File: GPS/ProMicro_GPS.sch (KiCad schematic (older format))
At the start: 32 parts, among them J1 uFL, J2 Coax, U1 SIM28ML, U2 MPU-9250

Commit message: add 1.8V for Gyro
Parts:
- added C10, C11: 100n, Capacitor_SMD:C_0402_1005Metric, symbol Device:C
- added H1: MountingHole, MountingHole:MountingHole_2.1mm, symbol Mechanical:MountingHole
- added U3: AP2112K-1.8, Package_TO_SOT_SMD:SOT-23-5, symbol Regulator_Linear:AP2112K-1.8
- A1: renamed from A?; symbol MCU_Module:Sparkfun_Pro_Micro_3V3 -> ProMicro:Sparkfun_Pro_Micro_3V3
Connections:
- net +3V3: now also C10.1, U3.1 (VIN), U3.3 (EN); no longer U2.8 (VDDIO)
- net GND: now also C10.2, C11.2, U3.2 (GND)
- new net +1V8: C11.1, U2.8 (VDDIO), U3.5 (VOUT)
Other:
- note removed: "Alternativ:\nICM-20948 requires 1.8V @VDDIO"
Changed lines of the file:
@@
 Title "ProMicro_GPS"
 Date "2020-05-30"
-Rev "v3"
+Rev "v3.1"
 Comp ""
 Comment1 ""
@@
 Wire Wire Line
 	3200 2000 3300 2000
-Wire Wire Line
-	3900 1000 3900 1100
 Wire Wire Line
 	4000 2900 4000 3000
@@
 L power:+3V3 #PWR06
 U 1 1 5E1569C8
-P 3200 1000
-F 0 "#PWR06" H 3200 850 50  0001 C CNN
-F 1 "+3V3" H 3200 1150 50  0000 C CNN
-F 2 "" H 3200 1000 50  0001 C CNN
-F 3 "" H 3200 1000 50  0001 C CNN
-	1    3200 1000
-	1    0    0    -1
-$EndComp
-$Comp
-L power:+3V3 #PWR07
-U 1 1 5E0EC300
-P 3900 1000
-F 0 "#PWR07" H 3900 850 50  0001 C CNN
-F 1 "+3V3" H 3900 1150 50  0000 C CNN
-F 2 "" H 3900 1000 50  0001 C CNN
-F 3 "" H 3900 1000 50  0001 C CNN
-	1    3900 1000
+P 1250 2150
+F 0 "#PWR06" H 1250 2000 50  0001 C CNN
+F 1 "+3V3" H 1250 2300 50  0000 C CNN
+F 2 "" H 1250 2150 50  0001 C CNN
+F 3 "" H 1250 2150 50  0001 C CNN
+	1    1250 2150
 	1    0    0    -1
 $EndComp
@@
 	1    0    0    -1
 $EndComp
-Text Notes 1750 2750 0    50   ~ 0
-Alternativ:\nICM-20948 requires 1.8V @VDDIO
 Text Notes 3250 6750 0    50   ~ 0
 Alternativ:\nMAX-8
@@
 NoConn ~ 8800 2000
 $Comp
-L MCU_Module:Sparkfun_Pro_Micro_3V3 A?
+L ProMicro:Sparkfun_Pro_Micro_3V3 A1
 U 1 1 5F52CC97
 P 8900 3000
-F 0 "A?" H 8900 4200 50  0000 C CNN
-F 1 "Sparkfun_Pro_Micro_3V3" H 8900 4100 50  0000 C CNN
+F 0 "A1" H 8550 3950 50  0000 C CNN
+F 1 "Sparkfun_Pro_Micro_3V3" H 9500 2050 50  0000 C CNN
 F 2 "Module:Sparkfun_Pro_Micro" H 8900 3000 50  0001 C CIN
 F 3 "https://www.sparkfun.com/products/12587" H 8900 2000 50  0001 C CNN
@@
 	1    0    0    -1
 $EndComp
+$Comp
+L power:+1V8 #PWR0103
+U 1 1 5F54927C
+P 2250 2150
+F 0 "#PWR0103" H 2250 2000 50  0001 C CNN
+F 1 "+1V8" H 2250 2300 50  0000 C CNN
+F 2 "" H 2250 2150 50  0001 C CNN
+F 3 "" H 2250 2150 50  0001 C CNN
+	1    2250 2150
+	1    0    0    -1
+$EndComp
+Wire Wire Line
+	3900 1000 3900 1100
+Wire Wire Line
+	1250 2150 1250 2300
+Wire Wire Line
+	1250 2300 1450 2300
+Wire Wire Line
+	2250 2150 2250 2300
+Wire Wire Line
+	2250 2300 2050 2300
+$Comp
+L Device:C C10
+U 1 1 5F551E51
+P 1250 2650
+F 0 "C10" H 1380 2700 50  0000 L CNN
+F 1 "100n" H 1380 2600 50  0000 L CNN
+F 2 "Capacitor_SMD:C_0402_1005Metric" H 1288 2500 50  0001 C CNN
+F 3 "~" H 1250 2650 50  0001 C CNN
+F 4 "CL05B104KO5NNNC" H 1250 2650 50  0001 C CNN "manf#"
+F 5 "GYRO" H 1250 2650 50  0001 C CNN "variant"
+F 6 "C1525" H 1250 2650 50  0001 C CNN "LCSC#"
+	1    1250 2650
+	1    0    0    -1
+$EndComp
+$Comp
+L Device:C C11
+U 1 1 5F552790
+P 2250 2650
+F 0 "C11" H 2380 2700 50  0000 L CNN
+F 1 "100n" H 2380 2600 50  0000 L CNN
+F 2 "Capacitor_SMD:C_0402_1005Metric" H 2288 2500 50  0001 C CNN
+F 3 "~" H 2250 2650 50  0001 C CNN
+F 4 "CL05B104KO5NNNC" H 2250 2650 50  0001 C CNN "manf#"
+F 5 "GYRO" H 2250 2650 50  0001 C CNN "variant"
+F 6 "C1525" H 2250 2650 50  0001 C CNN "LCSC#"
+	1    2250 2650
+	1    0    0    -1
+$EndComp
+$Comp
+L power:GND #PWR0104
+U 1 1 5F552CA6
+P 1250 2900
+F 0 "#PWR0104" H 1250 2650 50  0001 C CNN
+F 1 "GND" H 1250 2750 50  0000 C CNN
+F 2 "" H 1250 2900 50  0001 C CNN
+F 3 "" H 1250 2900 50  0001 C CNN
+	1    1250 2900
+	1    0    0    -1
+$EndComp
+$Comp
+L power:GND #PWR0105
+U 1 1 5F55330E
+P 1750 2900
+F 0 "#PWR0105" H 1750 2650 50  0001 C CNN
+F 1 "GND" H 1750 2750 50  0000 C CNN
+F 2 "" H 1750 2900 50  0001 C CNN
+F 3 "" H 1750 2900 50  0001 C CNN
+	1    1750 2900
+	1    0    0    -1
+$EndComp
+$Comp
+L power:GND #PWR0106
+U 1 1 5F55357B
+P 2250 2900
+F 0 "#PWR0106" H 2250 2650 50  0001 C CNN
+F 1 "GND" H 2250 2750 50  0000 C CNN
+F 2 "" H 2250 2900 50  0001 C CNN
+F 3 "" H 2250 2900 50  0001 C CNN
+	1    2250 2900
+	1    0    0    -1
+$EndComp
+Connection ~ 1250 2300
+Wire Wire Line
+	1250 2900 1250 2800
+Wire Wire Line
+	1750 2700 1750 2900
+Wire Wire Line
+	2250 2900 2250 2800
+Connection ~ 2250 2300
+$Comp
+L power:+1V8 #PWR0107
+U 1 1 5F56BB7F
+P 3900 1000
+F 0 "#PWR0107" H 3900 850 50  0001 C CNN
+F 1 "+1V8" H 3900 1150 50  0000 C CNN
+F 2 "" H 3900 1000 50  0001 C CNN
+F 3 "" H 3900 1000 50  0001 C CNN
+	1    3900 1000
+	1    0    0    -1
+$EndComp
+$Comp
+L power:+3V3 #PWR0108
+U 1 1 5F56BF74
+P 3200 1000
+F 0 "#PWR0108" H 3200 850 50  0001 C CNN
+F 1 "+3V3" H 3200 1150 50  0000 C CNN
+F 2 "" H 3200 1000 50  0001 C CNN
+F 3 "" H 3200 1000 50  0001 C CNN
+	1    3200 1000
+	1    0    0    -1
+$EndComp
+$Comp
+L Regulator_Linear:AP2112K-1.8 U3
+U 1 1 5F56F1F1
+P 1750 2400
+F 0 "U3" H 1775 2800 50  0000 C CNN
+F 1 "AP2112K-1.8" H 1775 2700 50  0000 C CNN
+F 2 "Package_TO_SOT_SMD:SOT-23-5" H 1750 2725 50  0001 C CNN
+F 3 "https://www.diodes.com/assets/Datasheets/AP2112.pdf" H 1750 2500 50  0001 C CNN
+	1    1750 2400
+	1    0    0    -1
+$EndComp
+Wire Wire Line
+	2250 2300 2250 2500
+Wire Wire Line
+	1450 2400 1250 2400
+Wire Wire Line
+	1250 2300 1250 2400
+Wire Wire Line
+	1250 2400 1250 2500
+Connection ~ 1250 2400
+$Comp
+L Mechanical:MountingHole H1
+U 1 1 5F549B76
+P 5750 4750
+F 0 "H1" H 5850 4825 50  0000 L CNN
+F 1 "MountingHole" H 5850 4725 50  0000 L CNN
+F 2 "MountingHole:MountingHole_2.1mm" H 5750 4750 50  0001 C CNN
+F 3 "~" H 5750 4750 50  0001 C CNN
+	1    5750 4750
+	1    0    0    -1
+$EndComp

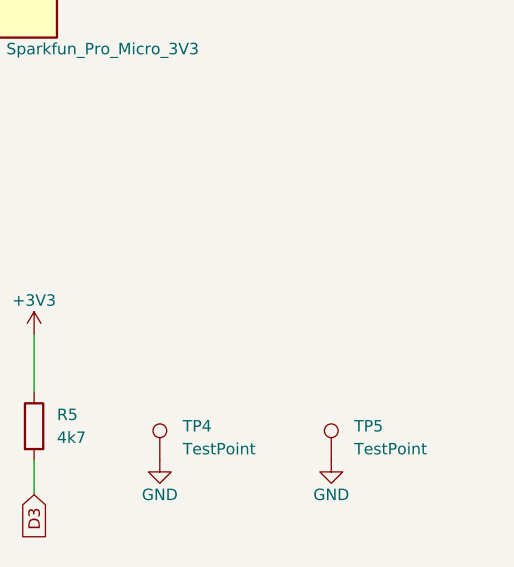
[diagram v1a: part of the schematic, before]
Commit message: adding holes for antenna
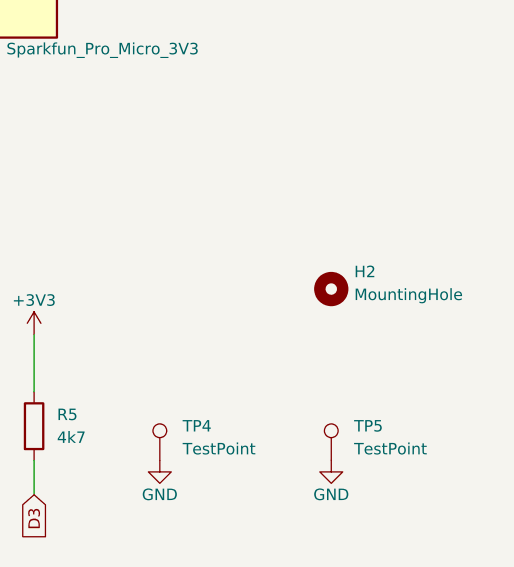
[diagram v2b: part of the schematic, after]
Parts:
- added H2: MountingHole, MountingHole:MountingHole_2.1mm, symbol Mechanical:MountingHole
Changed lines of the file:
@@
 Sheet 1 1
 Title "ProMicro_GPS"
-Date "2020-05-30"
+Date "2020-09-05"
 Rev "v3.1"
 Comp ""
@@
 	1    0    0    -1
 $EndComp
+$Comp
+L Mechanical:MountingHole H2
+U 1 1 5F544468
+P 10500 5000
+F 0 "H2" H 10600 5075 50  0000 L CNN
+F 1 "MountingHole" H 10600 4975 50  0000 L CNN
+F 2 "MountingHole:MountingHole_2.1mm" H 10500 5000 50  0001 C CNN
+F 3 "~" H 10500 5000 50  0001 C CNN
+	1    10500 5000
+	1    0    0    -1
+$EndComp

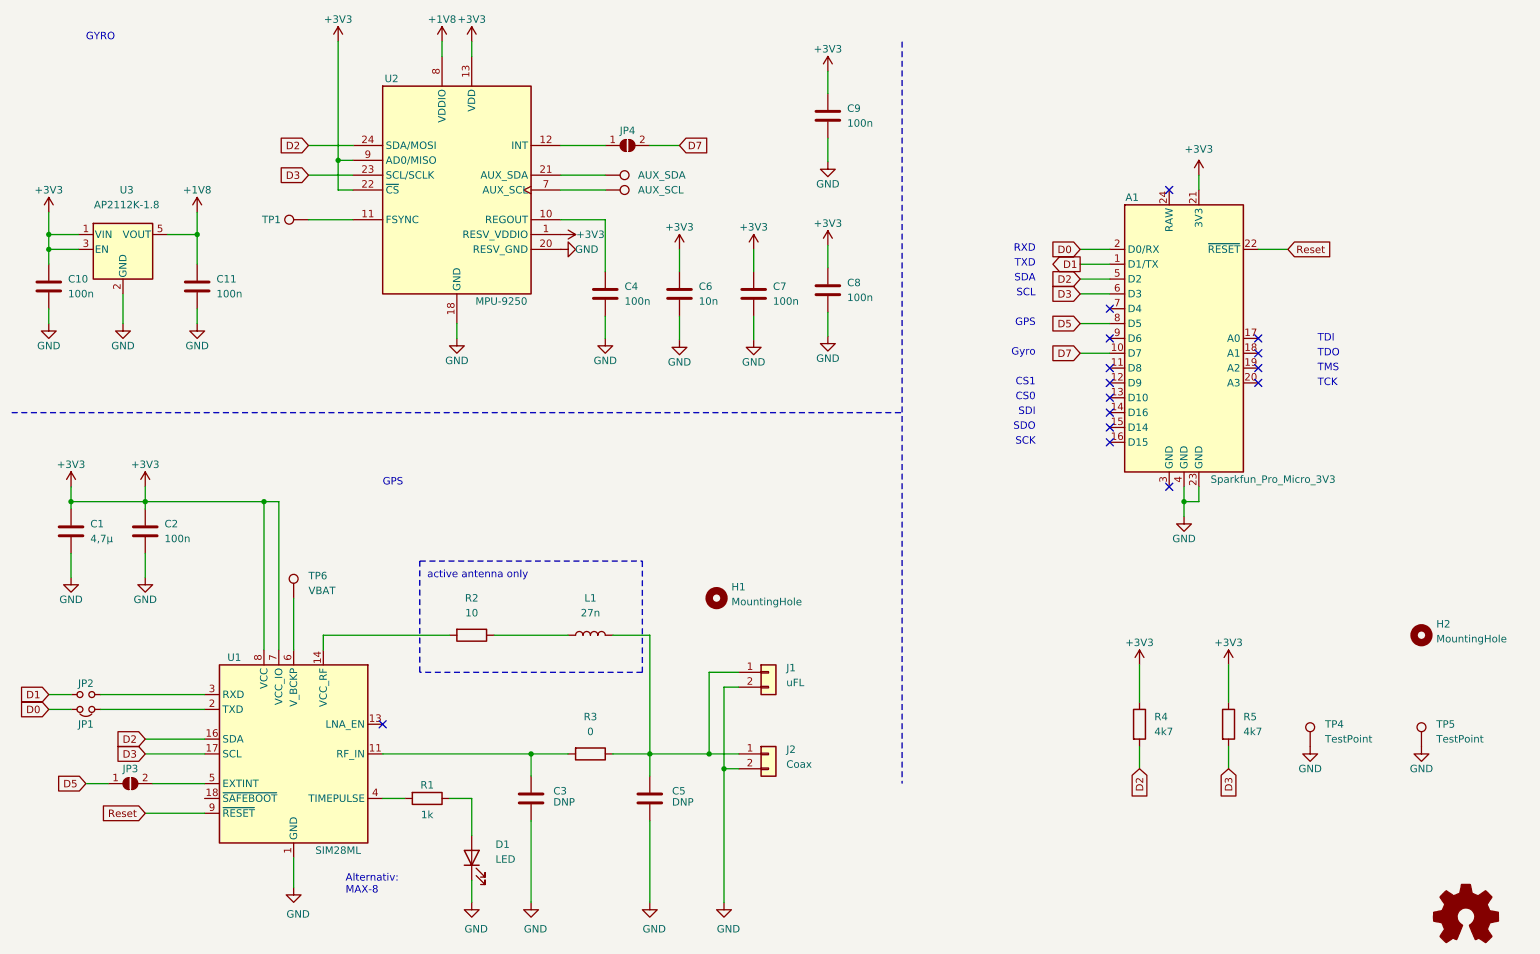
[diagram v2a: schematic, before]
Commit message: changed signal names
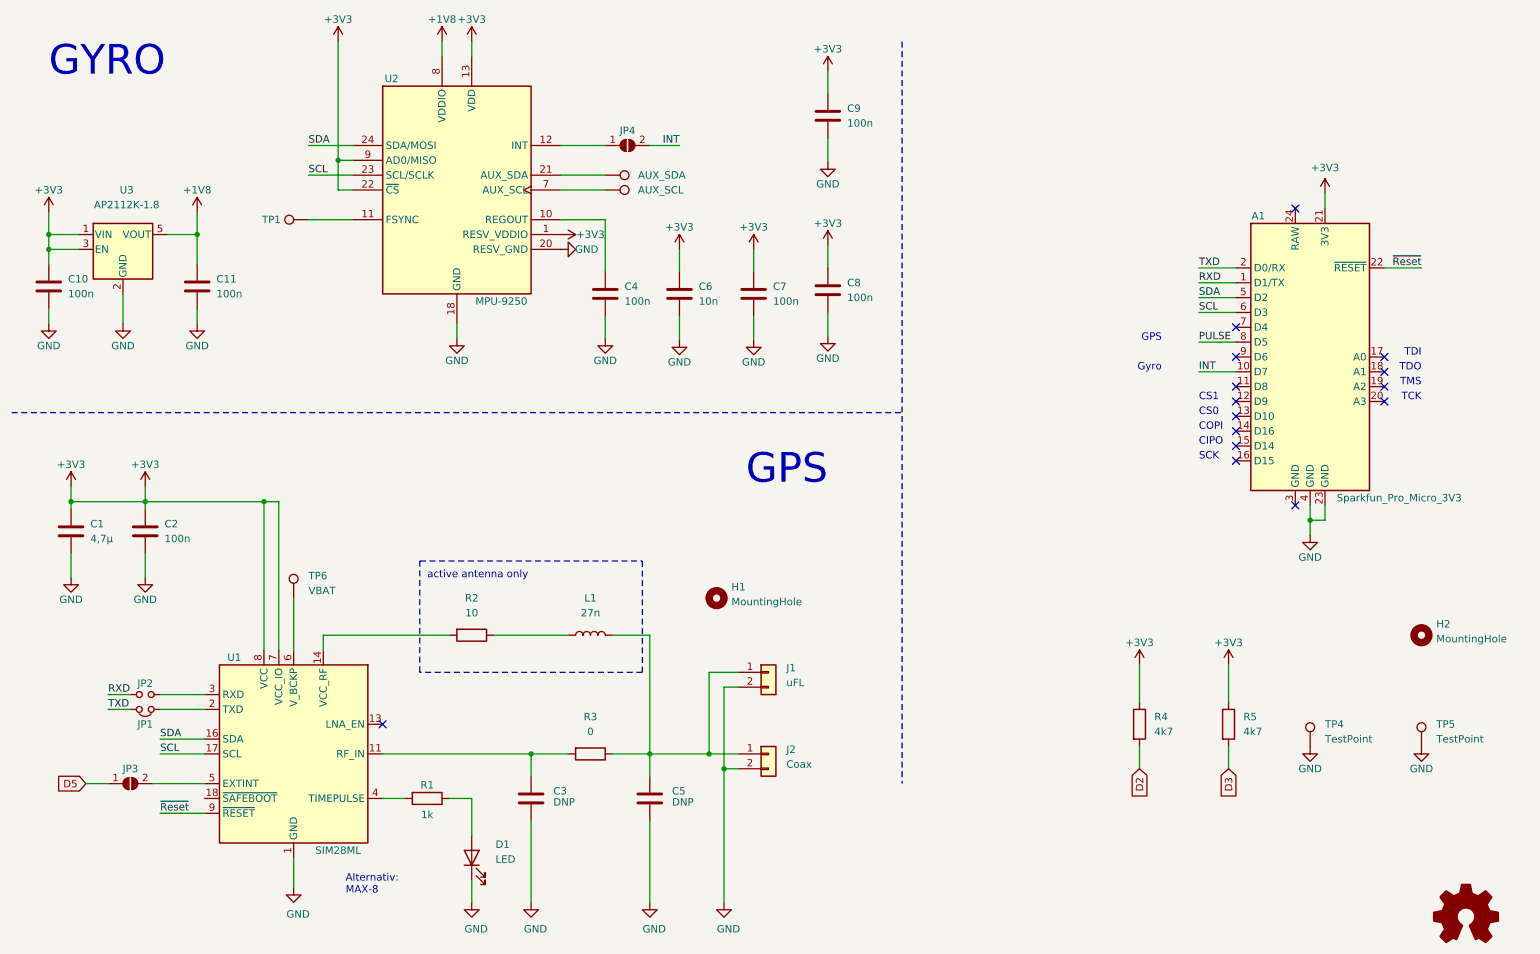
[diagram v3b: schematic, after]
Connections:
- net D2: no longer A1.5 (D2), U1.16 (SDA), U2.24 (SDA/MOSI)
- net D3: no longer A1.6 (D3), U1.17 (SCL), U2.23 (SCL/SCLK)
- net D5: no longer A1.8 (D5)
- net D0 renamed TXD
- net D1 renamed RXD
- net D7 renamed INT
- net Reset renamed ~Reset
- new net PULSE: A1.8 (D5)
- new net SCL: A1.6 (D3), U1.17 (SCL), U2.23 (SCL/SCLK)
- new net SDA: A1.5 (D2), U1.16 (SDA), U2.24 (SDA/MOSI)
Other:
- note added: "CIPO"
- note added: "COPI"
- note removed: "RXD"
- note removed: "SCL"
- note removed: "SDA"
- note removed: "SDI"
- note removed: "SDO"
- note removed: "TXD"
- moved on the sheet: A1, JP1, JP2
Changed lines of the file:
@@
 Title "ProMicro_GPS"
 Date "2020-09-05"
-Rev "v3.1"
+Rev "v3.2"
 Comp ""
 Comment1 ""
@@
 	1950 6000 2300 6000
 Wire Wire Line
-	1900 5700 2300 5700
-Wire Wire Line
-	1900 5800 2300 5800
-Wire Wire Line
-	1900 6200 2300 6200
-Wire Wire Line
 	5300 5800 5700 5800
 Wire Wire Line
@@
 Text GLabel 1500 6000 0    50   Input ~ 0
 D5
-Text GLabel 1250 5400 0    50   Input ~ 0
-D1
-Text GLabel 1250 5500 0    50   Input ~ 0
-D0
-Text GLabel 1900 5700 0    50   Input ~ 0
-D2
-Text GLabel 1900 5800 0    50   Input ~ 0
-D3
-Text GLabel 1900 6200 0    50   Input ~ 0
-Reset
 $Comp
 L power:+3V3 #PWR01
@@
 	1    0    0    -1
 $EndComp
-Connection ~ 8900 4100
+Connection ~ 9750 4225
 Wire Wire Line
 	3200 2000 3300 2000
@@
 	4100 1000 4100 1100
 Wire Wire Line
-	8900 4000 8900 4100
-Wire Wire Line
-	8900 4100 8900 4200
-Wire Wire Line
-	9000 1900 9000 2000
-Wire Wire Line
-	9000 4000 9000 4100
-Wire Wire Line
-	9000 4100 8900 4100
+	9750 4125 9750 4225
+Wire Wire Line
+	9750 4225 9750 4325
+Wire Wire Line
+	9850 2025 9850 2125
+Wire Wire Line
+	9850 4125 9850 4225
+Wire Wire Line
+	9850 4225 9750 4225
 Wire Wire Line
 	5500 2400 5500 2550
@@
 Wire Wire Line
 	6000 2850 6000 3010
-Wire Wire Line
-	8200 2400 8400 2400
-Wire Wire Line
-	8200 2500 8400 2500
-Wire Wire Line
-	8200 2600 8400 2600
-Wire Wire Line
-	8200 2700 8400 2700
-Wire Wire Line
-	8200 2900 8400 2900
-Wire Wire Line
-	8200 3100 8400 3100
-Wire Wire Line
-	9400 2400 9600 2400
 Wire Wire Line
 	8600 5450 8600 5200
@@
 Wire Notes Line
 	1000 3500 7000 3500
-Text Notes 9800 3030 0    50   ~ 0
+Text Notes 10500 3125 2    50   ~ 0
 TDI
-Text Notes 9800 3130 0    50   ~ 0
+Text Notes 10500 3225 2    50   ~ 0
 TDO
-Text Notes 9800 3230 0    50   ~ 0
+Text Notes 10500 3325 2    50   ~ 0
 TMS
-Text Notes 9800 3330 0    50   ~ 0
+Text Notes 10500 3425 2    50   ~ 0
 TCK
-Text GLabel 3000 1700 0    50   Input ~ 0
-D2
-Text GLabel 3000 1900 0    50   Input ~ 0
-D3
-Text GLabel 8200 2400 0    50   Input ~ 0
-D0
-Text GLabel 8200 2500 0    50   Output ~ 0
-D1
-Text GLabel 8200 2600 0    50   Input ~ 0
-D2
-Text GLabel 8200 2900 0    50   Input ~ 0
-D5
-Text GLabel 8200 3100 0    50   Input ~ 0
-D7
 Text GLabel 8600 5900 3    50   Input ~ 0
 D2
 Text GLabel 9200 5900 3    50   Input ~ 0
 D3
-Text GLabel 9600 2400 2    50   Input ~ 0
-Reset
 $Comp
 L Connector:TestPoint TP1
@@
 L power:+3V3 #PWR025
 U 1 1 5E126446
-P 9000 1900
-F 0 "#PWR025" H 9000 1750 50  0001 C CNN
-F 1 "+3V3" H 9000 2075 50  0000 C CNN
-F 2 "" H 9000 1900 50  0001 C CNN
-F 3 "" H 9000 1900 50  0001 C CNN
-	1    9000 1900
+P 9850 2025
+F 0 "#PWR025" H 9850 1875 50  0001 C CNN
+F 1 "+3V3" H 9850 2200 50  0000 C CNN
+F 2 "" H 9850 2025 50  0001 C CNN
+F 3 "" H 9850 2025 50  0001 C CNN
+	1    9850 2025
 	1    0    0    -1
 $EndComp
@@
 L power:GND #PWR024
 U 1 1 5E53883D
-P 8900 4200
-F 0 "#PWR024" H 8900 3950 50  0001 C CNN
-F 1 "GND" H 8900 4050 50  0000 C CNN
-F 2 "" H 8900 4200 50  0001 C CNN
-F 3 "" H 8900 4200 50  0001 C CNN
-	1    8900 4200
+P 9750 4325
+F 0 "#PWR024" H 9750 4075 50  0001 C CNN
+F 1 "GND" H 9750 4175 50  0000 C CNN
+F 2 "" H 9750 4325 50  0001 C CNN
+F 3 "" H 9750 4325 50  0001 C CNN
+	1    9750 4325
 	1    0    0    -1
 $EndComp
@@
 	1    0    0    -1
 $EndComp
-Text GLabel 8200 2700 0    50   Input ~ 0
-D3
-Text Notes 7900 2725 2    50   ~ 0
-SCL
-Text Notes 7900 2625 2    50   ~ 0
-SDA
-Text Notes 7900 2525 2    50   ~ 0
-TXD
-Text Notes 7900 2425 2    50   ~ 0
-RXD
-Text Notes 7900 3725 2    50   ~ 0
+Text Notes 9000 3825 0    50   ~ 0
 SCK
-Text Notes 7900 3625 2    50   ~ 0
-SDO
-Text Notes 7900 3525 2    50   ~ 0
-SDI
-Text Notes 7900 3425 2    50   ~ 0
+Text Notes 9000 3725 0    50   ~ 0
+CIPO
+Text Notes 9000 3625 0    50   ~ 0
+COPI
+Text Notes 9000 3525 0    50   ~ 0
 CS0
-Text Notes 7900 3325 2    50   ~ 0
+Text Notes 9000 3425 0    50   ~ 0
 CS1
 Wire Wire Line
@@
 Wire Wire Line
 	3200 1800 3200 2000
-NoConn ~ 8800 4000
+NoConn ~ 9650 4125
 $Comp
 L Sensor_Motion:MPU-9250 U2
@@
 	1    0    0    -1
 $EndComp
-Text GLabel 5500 1700 2    50   Input ~ 0
-D7
 Wire Wire Line
 	4700 1700 5000 1700
-Text Notes 7900 3125 2    50   ~ 0
+Text Notes 8750 3225 2    50   ~ 0
 Gyro
 $Comp
@@
 	1    0    0    -1
 $EndComp
-Text Notes 7900 2925 2    50   ~ 0
+Text Notes 8750 3025 2    50   ~ 0
 GPS
 $Comp
@@
 	1    0    0    -1
 $EndComp
-Text Notes 1500 1000 0    50   ~ 0
+Text Notes 1250 1250 0    200  ~ 0
 GYRO
-Text Notes 3500 4000 0    50   ~ 0
+Text Notes 6500 4000 2    200  ~ 0
 GPS
 $Comp
 L Device:Jumper_NO_Small JP2
 U 1 1 5E617C03
-P 1500 5400
-F 0 "JP2" H 1500 5325 50  0000 C CNN
-F 1 "Jumper_NO_Small" H 1525 5500 50  0001 C CNN
-F 2 "Jumper:SolderJumper-2_P1.3mm_Open_RoundedPad1.0x1.5mm" H 1500 5400 50  0001 C CNN
-F 3 "~" H 1500 5400 50  0001 C CNN
-F 4 "DNP" H 1500 5400 50  0001 C CNN "variant"
-	1    1500 5400
+P 1900 5400
+F 0 "JP2" H 1900 5325 50  0000 C CNN
+F 1 "Jumper_NO_Small" H 1925 5500 50  0001 C CNN
+F 2 "Jumper:SolderJumper-2_P1.3mm_Open_RoundedPad1.0x1.5mm" H 1900 5400 50  0001 C CNN
+F 3 "~" H 1900 5400 50  0001 C CNN
+F 4 "DNP" H 1900 5400 50  0001 C CNN "variant"
+	1    1900 5400
 	-1   0    0    1
 $EndComp
 Wire Wire Line
-	1600 5500 2300 5500
-Wire Wire Line
-	1250 5500 1400 5500
+	1650 5500 1800 5500
 $Comp
 L Device:Jumper_NC_Small JP1
 U 1 1 5E620A66
-P 1500 5500
-F 0 "JP1" H 1500 5600 50  0000 C CNN
-F 1 "Jumper_NC_Small" H 1525 5625 50  0001 C CNN
-F 2 "Jumper:SolderJumper-2_P1.3mm_Bridged_RoundedPad1.0x1.5mm" H 1500 5500 50  0001 C CNN
-F 3 "~" H 1500 5500 50  0001 C CNN
-F 4 "DNP" H 1500 5500 50  0001 C CNN "variant"
-	1    1500 5500
+P 1900 5500
+F 0 "JP1" H 1900 5600 50  0000 C CNN
+F 1 "Jumper_NC_Small" H 1925 5625 50  0001 C CNN
+F 2 "Jumper:SolderJumper-2_P1.3mm_Bridged_RoundedPad1.0x1.5mm" H 1900 5500 50  0001 C CNN
+F 3 "~" H 1900 5500 50  0001 C CNN
+F 4 "DNP" H 1900 5500 50  0001 C CNN "variant"
+	1    1900 5500
 	-1   0    0    1
 $EndComp
 Wire Wire Line
-	1250 5400 1400 5400
-Wire Wire Line
-	1600 5400 2300 5400
+	1650 5400 1800 5400
 Wire Notes Line
 	3750 5250 3750 4500
@@
 Text Notes 3250 6750 0    50   ~ 0
 Alternativ:\nMAX-8
-NoConn ~ 8400 2800
-NoConn ~ 8400 3000
-NoConn ~ 8400 3200
-NoConn ~ 8400 3300
-NoConn ~ 8400 3400
-NoConn ~ 8400 3500
-NoConn ~ 8400 3600
-NoConn ~ 8400 3700
-NoConn ~ 9400 3300
-NoConn ~ 9400 3200
-NoConn ~ 9400 3100
-NoConn ~ 9400 3000
-NoConn ~ 8800 2000
+NoConn ~ 9250 2925
+NoConn ~ 9250 3125
+NoConn ~ 9250 3325
+NoConn ~ 9250 3425
+NoConn ~ 9250 3525
+NoConn ~ 9250 3625
+NoConn ~ 9250 3725
+NoConn ~ 9250 3825
+NoConn ~ 10250 3425
+NoConn ~ 10250 3325
+NoConn ~ 10250 3225
+NoConn ~ 10250 3125
+NoConn ~ 9650 2125
 $Comp
 L ProMicro:Sparkfun_Pro_Micro_3V3 A1
 U 1 1 5F52CC97
-P 8900 3000
-F 0 "A1" H 8550 3950 50  0000 C CNN
-F 1 "Sparkfun_Pro_Micro_3V3" H 9500 2050 50  0000 C CNN
-F 2 "Module:Sparkfun_Pro_Micro" H 8900 3000 50  0001 C CIN
-F 3 "https://www.sparkfun.com/products/12587" H 8900 2000 50  0001 C CNN
-	1    8900 3000
+P 9750 3125
+F 0 "A1" H 9400 4075 50  0000 C CNN
+F 1 "Sparkfun_Pro_Micro_3V3" H 10350 2175 50  0000 C CNN
+F 2 "Module:Sparkfun_Pro_Micro" H 9750 3125 50  0001 C CIN
+F 3 "https://www.sparkfun.com/products/12587" H 9750 2125 50  0001 C CNN
+	1    9750 3125
 	1    0    0    -1
 $EndComp
@@
 	1    0    0    -1
 $EndComp
+Wire Wire Line
+	9000 2625 9250 2625
+Wire Wire Line
+	9000 2525 9250 2525
+Text Label 9000 2525 0    50   ~ 0
+TXD
+Text Label 9000 2625 0    50   ~ 0
+RXD
+Wire Wire Line
+	10250 2525 10500 2525
+Text Label 10500 2525 2    50   ~ 0
+~Reset
+Wire Wire Line
+	9000 2725 9250 2725
+Wire Wire Line
+	9000 2825 9250 2825
+Text Label 9000 2725 0    50   ~ 0
+SDA
+Text Label 9000 2825 0    50   ~ 0
+SCL
+Text Label 3000 1700 0    50   ~ 0
+SDA
+Text Label 3000 1900 0    50   ~ 0
+SCL
+Wire Wire Line
+	2300 5700 2000 5700
+Wire Wire Line
+	2300 5800 2000 5800
+Text Label 2000 5700 0    50   ~ 0
+SDA
+Text Label 2000 5800 0    50   ~ 0
+SCL
+Wire Wire Line
+	2300 6200 2000 6200
+Text Label 2000 6200 0    50   ~ 0
+~Reset
+Wire Wire Line
+	2000 5500 2300 5500
+Wire Wire Line
+	2300 5400 2000 5400
+Text Label 1650 5400 0    50   ~ 0
+RXD
+Text Label 1650 5500 0    50   ~ 0
+TXD
+Wire Wire Line
+	9000 3225 9250 3225
+Text Label 9000 3225 0    50   ~ 0
+INT
+Text Label 5500 1700 2    50   ~ 0
+INT
+Wire Wire Line
+	9000 3025 9250 3025
+Text Label 9000 3025 0    50   ~ 0
+PULSE
 $EndSCHEMATC
